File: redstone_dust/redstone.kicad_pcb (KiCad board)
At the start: 2 copper layers, 72 parts, among them J1 1x4_Pogo, J2 1x4_Pogo, J3 1x4_Pogo, J4 1x4_Pogo, J5 1x4_Pogo, J6 1x4_Pogo, J7 1x4_Pogo, J8 1x4_Pogo, J9 2.54mm_ProgrammingPin, Q1 BC108, Q2 BC108, Q3 BC108, Q4 BC108, SW1 SW_Push_Open, U1 RP2040, U2 RBT05W24S05, U3 TPS62162DSG, U5 W25Q16JVSS

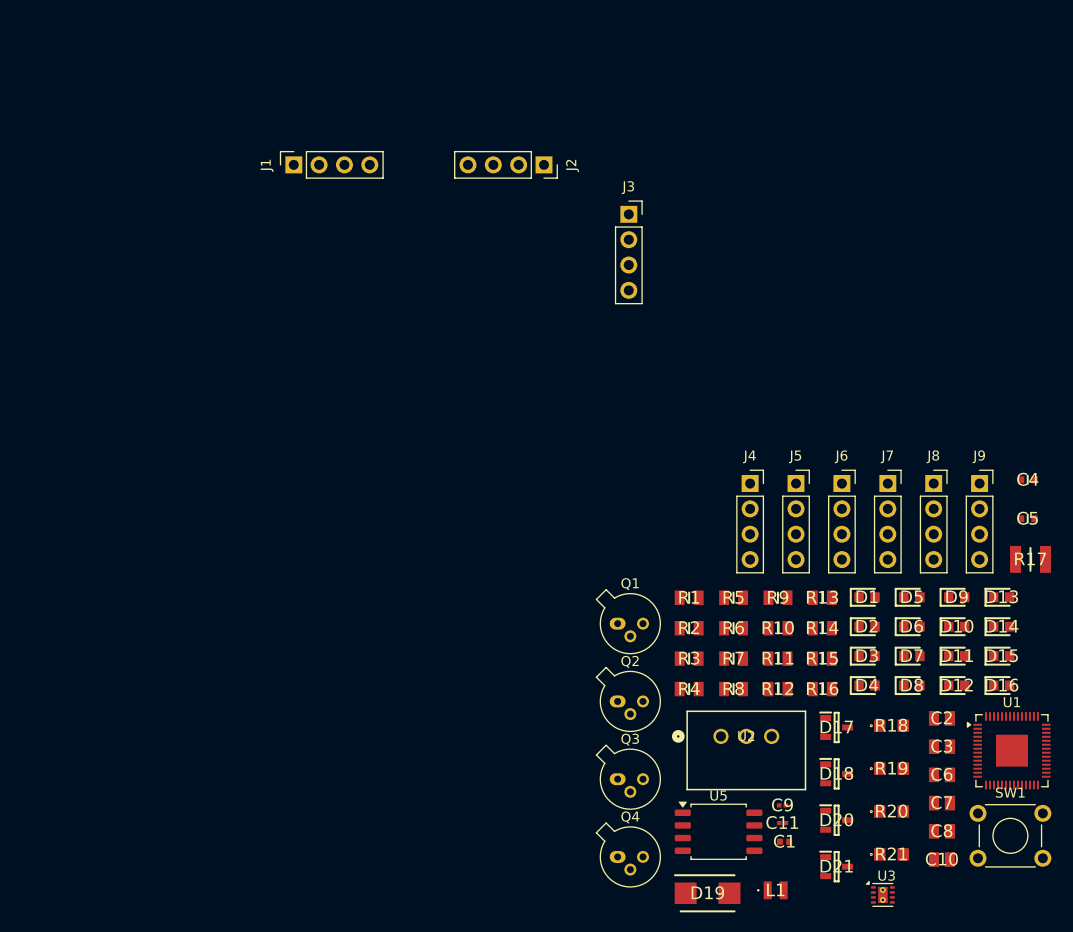
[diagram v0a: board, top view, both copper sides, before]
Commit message: add basic pcb layout, fix disconnected ground net
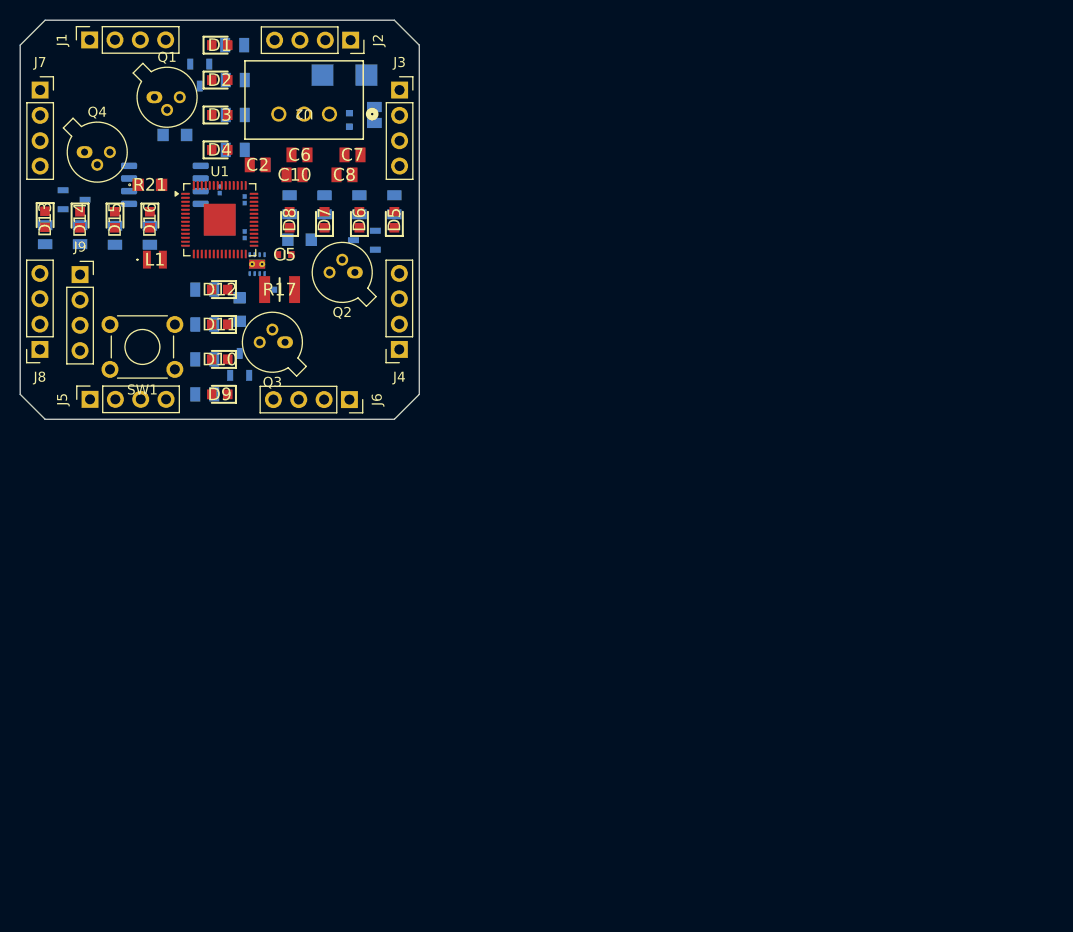
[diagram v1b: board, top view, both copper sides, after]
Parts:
- added C11: 1uF, SamacSys_Parts:CAPC0603X33N, B.Cu at (92.5, 53.0)
- C1, C11, C3, C4, C9, D17, D18, D19, D20, D21, R1, R10, R11, R12, R13, R14, R15, R16, R18, R19, R2, R20, R3, R4, R5, R6, R7, R8, R9, U3, U5: moved to B.Cu
- moved D13 103.1 mm to (72.5, 55.0), turned to -90 degrees
- moved D21 101.5 mm to (75.4, 53.0)
- moved D14 101.0 mm to (76.0, 55.0), turned to -90 degrees
- moved R21 100.1 mm to (83.0, 51.5)
- moved D15 99.1 mm to (79.5, 55.0), turned to -90 degrees
- moved D16 97.3 mm to (83.0, 55.0), turned to -90 degrees
- moved U1 95.6 mm to (90.0, 55.0)
- moved C10 94.4 mm to (97.5, 50.5)
- moved J7 93.7 mm to (72.0, 42.0)
- moved R18 93.1 mm to (85.5, 46.5)
- moved J9 92.6 mm to (76.0, 60.5)
- moved SW1 92.0 mm to (85.5, 70.0), turned to 180 degrees
- moved D17 91.4 mm to (88.0, 40.5), turned to -90 degrees
- moved J8 90.6 mm to (72.0, 68.0), turned to 180 degrees
- moved D19 89.7 mm to (102.5, 40.5)
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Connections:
- C1 pad 2: Net-(U3-AGND) -> GND
- C5 pad 2: Net-(U3-AGND) -> GND
- U3 pad 1: Net-(U3-AGND) -> GND
- U3 pad 4: Net-(U3-AGND) -> GND
- U3 pad 5: Net-(U3-AGND) -> GND
- U3 pad 9: Net-(U3-AGND) -> GND
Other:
- board outline added: 40 x 40 mm

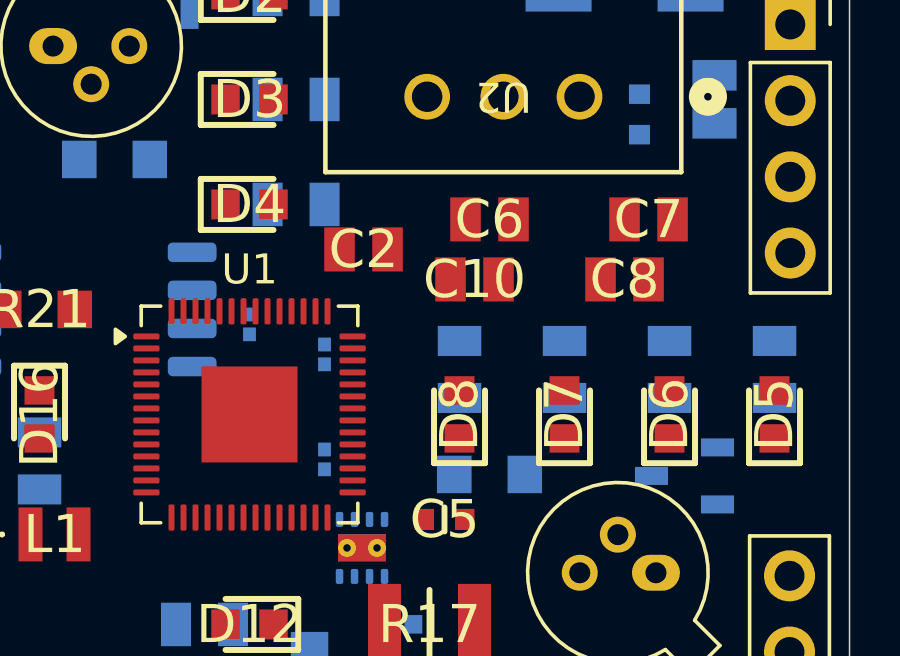
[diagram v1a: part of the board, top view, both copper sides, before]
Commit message: remove some unecessary capacitors
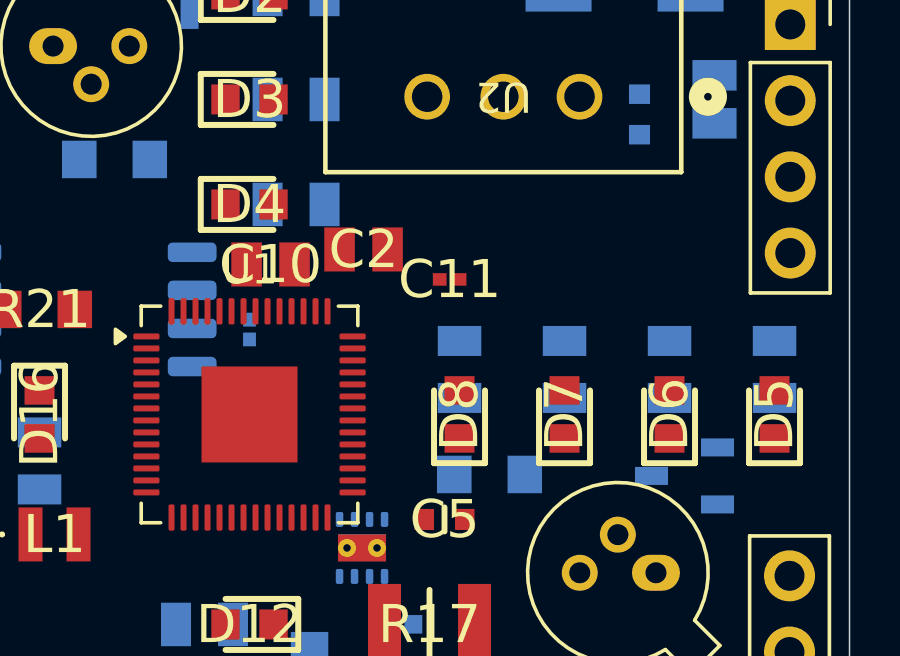
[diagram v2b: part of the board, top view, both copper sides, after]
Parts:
- removed the C11 at (92.5, 53.0)
- removed the C11 at (92.5, 56.5)
- removed C6, C7, C8: 0.1uF, SamacSys_Parts:CAPC2012X140N
- added C11: 1uF, SamacSys_Parts:CAPC0603X33N, F.Cu at (96.7, 50.5)
- moved C10 6.82 mm to (90.7, 50.0)
- moved C9 0.17 mm to (90.0, 52.2)

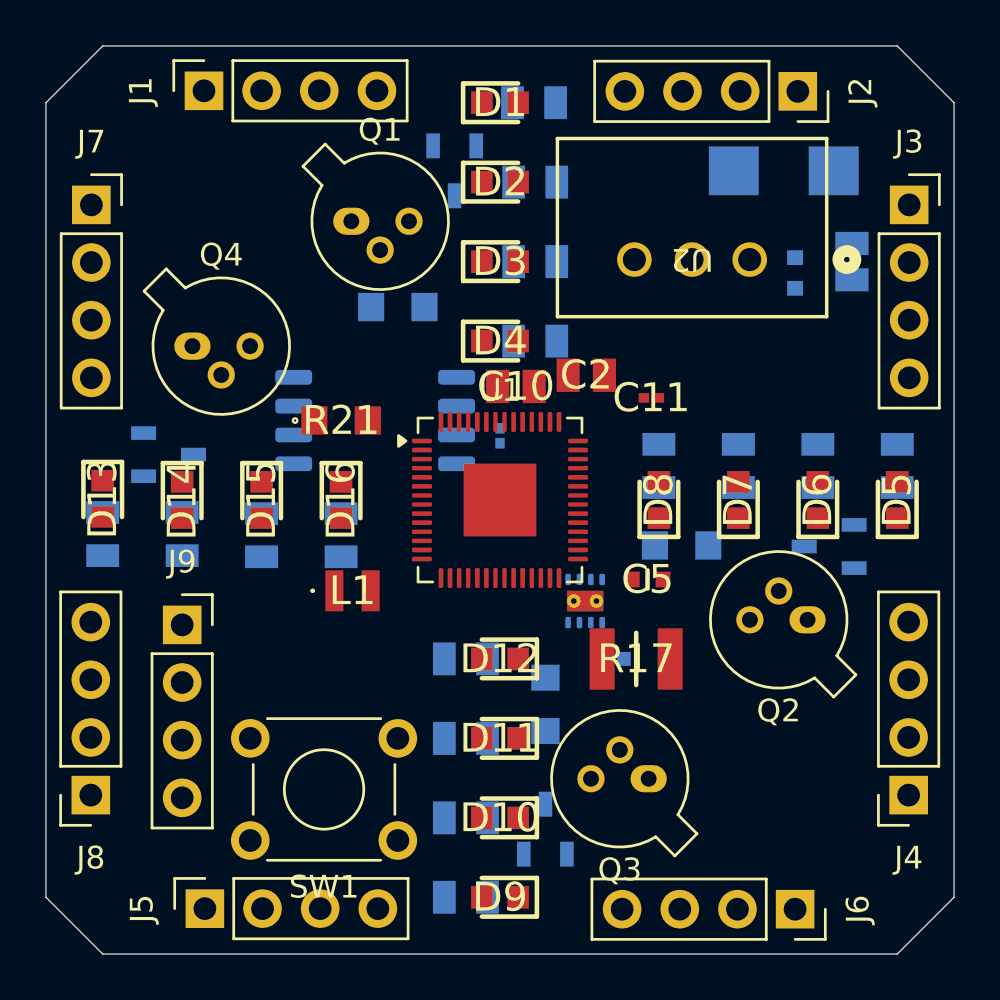
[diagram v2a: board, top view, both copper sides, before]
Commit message: add very bad traces, most likely will redo pcb layout
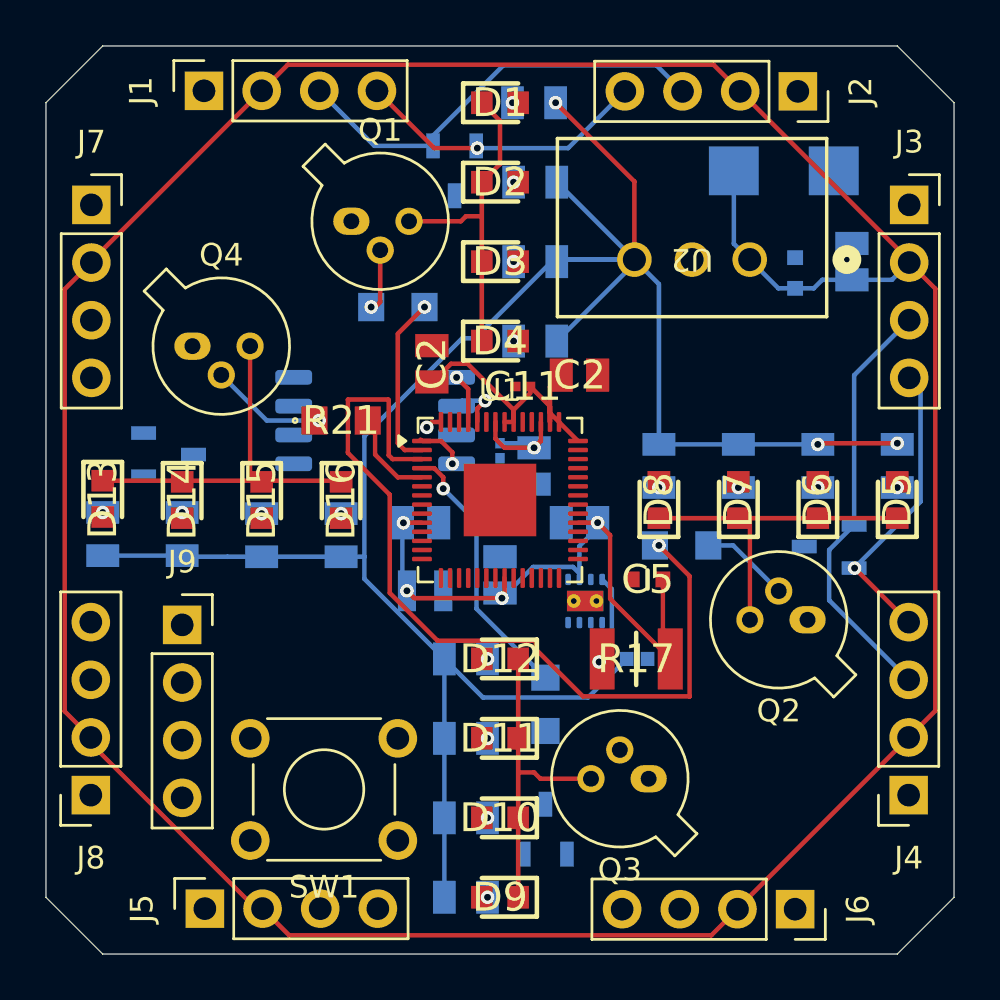
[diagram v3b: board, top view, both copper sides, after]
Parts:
- added C2: 0.1uF, SamacSys_Parts:CAPC2012X140N, F.Cu at (87.0, 49.0)
- added C2: 0.1uF, SamacSys_Parts:CAPC2012X140N, B.Cu at (93.5, 56.0)
- added C2: 0.1uF, SamacSys_Parts:CAPC2012X140N, B.Cu at (90.0, 58.3)
- added C2: 0.1uF, SamacSys_Parts:CAPC2012X140N, B.Cu at (86.5, 56.0)
- C10, L1: moved to B.Cu
- moved C11 5.69 mm to (91.0, 50.0), turned to 180 degrees
- moved C10 3.59 mm to (91.5, 53.5), turned to -90 degrees
- moved L1 3.20 mm to (86.7, 59.0)
- moved C1 1.04 mm to (96.0, 62.0)
- moved C9 0.66 mm to (90.0, 52.8)
- moved C2 0.30 mm to (93.5, 49.5)
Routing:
- net VCC: track 0.00 -> 142.7 mm
- net /5V_LOCAL: track 0.00 -> 98.8 mm, vias 0 -> 3
- net /3.3V_LOCAL: track 0.00 -> 44.5 mm, vias 0 -> 5
- net Net-(U1-GPIO1): track 0.00 -> 37.8 mm, vias 0 -> 1
- net /N_TX: track 0.00 -> 19.2 mm
- net /E_TX: track 0.00 -> 18.7 mm
- net Net-(D13-K): track 0.00 -> 16.5 mm
- net Net-(D5-K): track 0.00 -> 15.0 mm
- net Net-(D1-K): track 0.00 -> 14.5 mm
- net Net-(D10-K): track 0.00 -> 13.8 mm
- net /E_RX: track 0.00 -> 13.3 mm, vias 0 -> 1
- net /N_RX: track 0.00 -> 13.0 mm, vias 0 -> 1
- net Net-(U1-GPIO2): track 0.00 -> 11.8 mm, vias 0 -> 1
- net Net-(U1-GPIO0): track 0.00 -> 7.67 mm, vias 0 -> 1
- net Net-(U1-VREG_VOUT): track 0.00 -> 5.45 mm, vias 0 -> 1
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
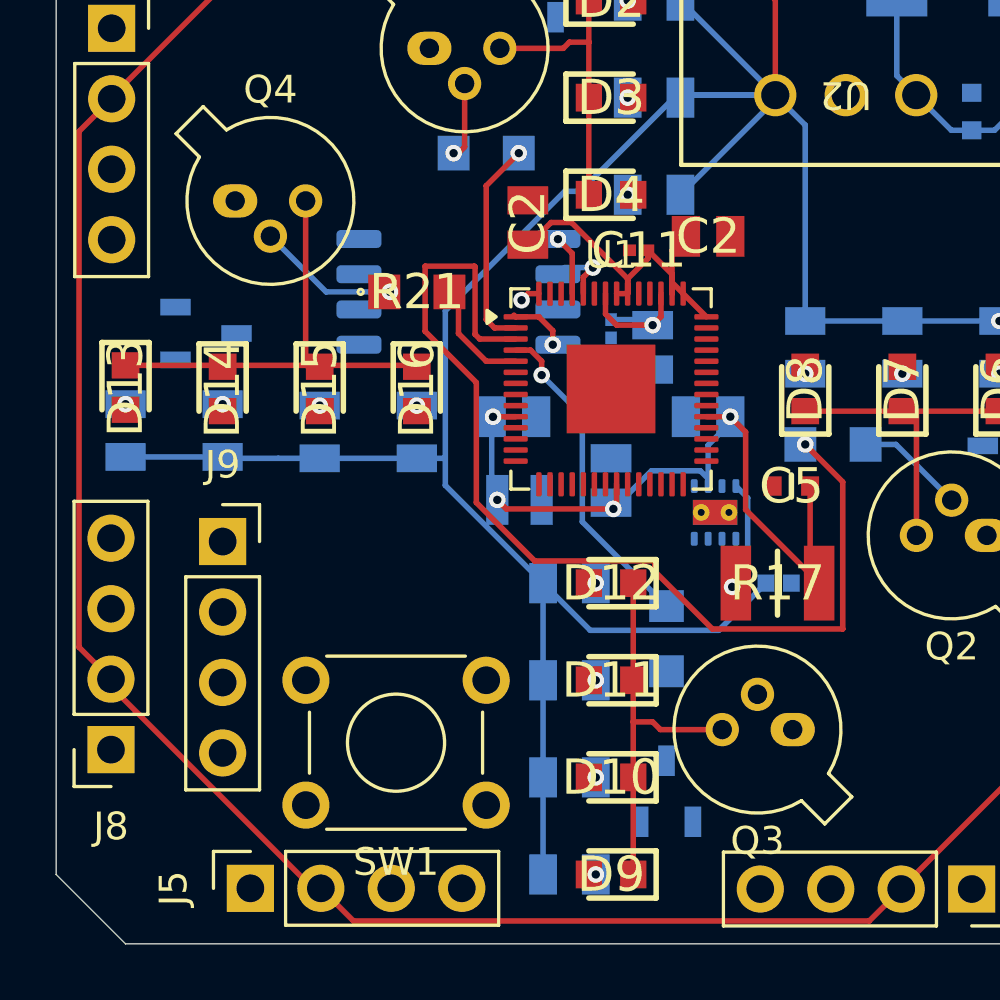
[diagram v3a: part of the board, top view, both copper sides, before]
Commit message: snapshot before removing all traces and restarting layout
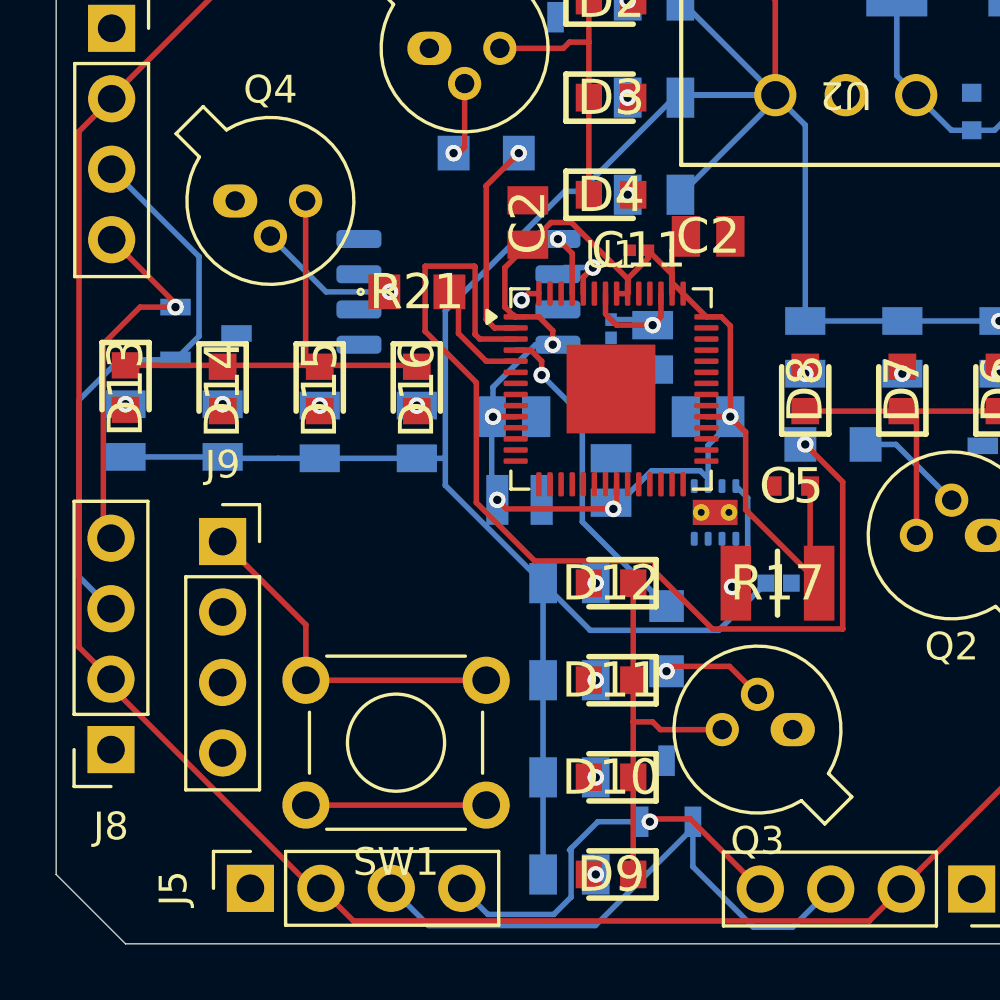
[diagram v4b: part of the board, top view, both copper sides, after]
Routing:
- net /S_TX: track 0.00 -> 21.2 mm
- net /W_TX: track 0.00 -> 20.6 mm
- net /3.3V_LOCAL: track 44.5 -> 62.5 mm
- net /S_RX: track 0.00 -> 14.4 mm, vias 0 -> 1
- net /W_RX: track 0.00 -> 13.7 mm, vias 0 -> 1
- net Net-(J9-Pin_1): track 0.00 -> 12.7 mm
- net Net-(Q3-B): track 0.00 -> 3.87 mm, vias 0 -> 1
